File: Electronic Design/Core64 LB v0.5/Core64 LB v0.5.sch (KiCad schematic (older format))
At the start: 14 parts, among them J12 TEENSY Cur. Mon., J4 PRG, U2 Teensy3.2

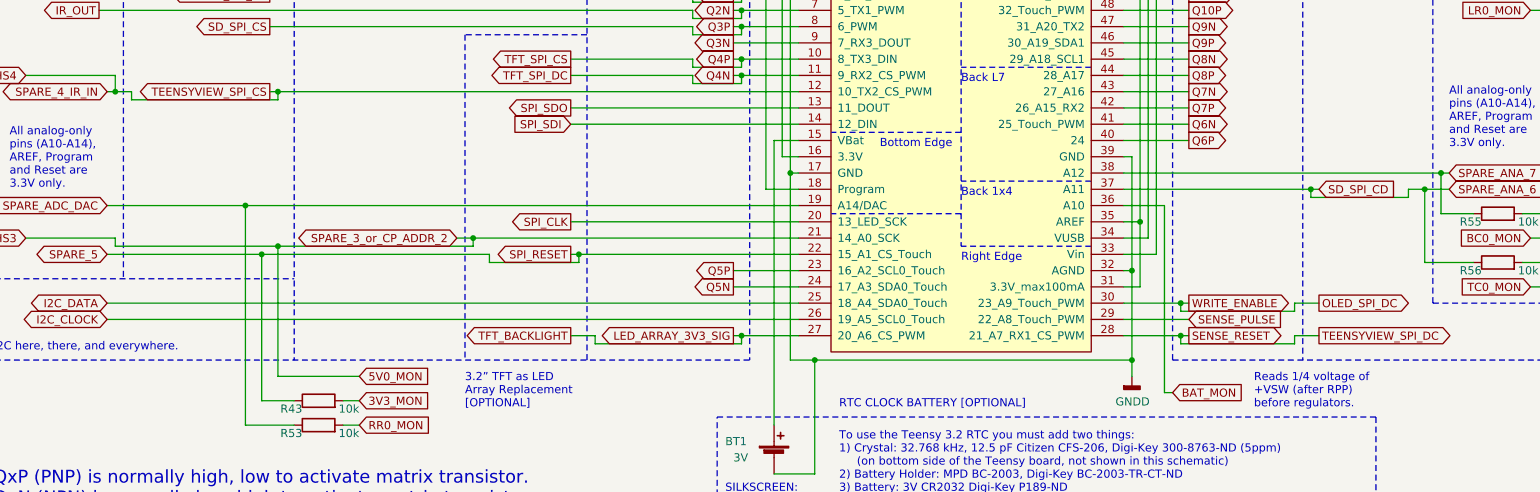
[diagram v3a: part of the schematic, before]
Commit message: Update schematic battery and LiPo charger notes, move SD_CD from ANA_6 to SPARE_3, schematic red lines
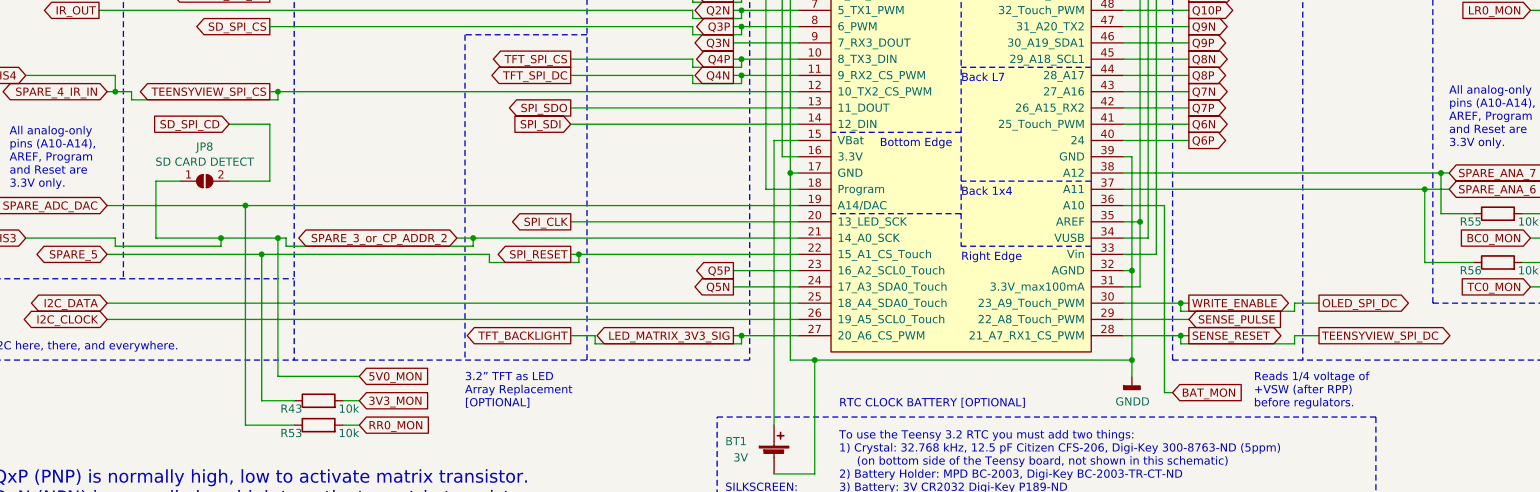
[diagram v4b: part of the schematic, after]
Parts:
- added JP8: SD CARD DETECT, Jumper:SolderJumper-2_P1.3mm_Open_RoundedPad1.0x1.5mm, symbol Jumper:SolderJumper_2_Open
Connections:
- net 5V0_MON: now also JP8.1 (A)
- net SD_SPI_CD: now also JP8.2 (B); no longer R56.1, U2.37 (A11)
- net LED_ARRAY_3V3_SIG renamed LED_MATRIX_3V3_SIG
- new net SPARE_ANA_6: R56.1, U2.37 (A11)
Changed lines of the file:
@@
 Date "2021-02-04"
 Rev "0.5"
-Comp "www.Core64.io"
-Comment1 "Work in progress"
-Comment2 "Andy Geppert"
+Comp "Concept and design by Andy Geppert @ www.MachineIdeas.com"
+Comment1 "Visit www.Core64.io for information on assembly and optional features."
+Comment2 "*** Work in progress ***"
 Comment3 ""
-Comment4 ""
+Comment4 "All non-polarized capacitors are X7R or X5R ceramic unless otherwise noted."
 $EndDescr
 Text Notes 2650 700  0    118  ~ 0
@@
 I2C_DATA
 Text GLabel 5250 5350 0    50   Output ~ 0
-LED_ARRAY_3V3_SIG
+LED_MATRIX_3V3_SIG
 $Sheet
 S 750  850  1450 250
@@
 Text GLabel 4250 4650 0    50   Output ~ 0
 SPI_CLK
-Text GLabel 8850 4450 2    50   Input ~ 0
+Text GLabel 2150 4050 0    50   Input ~ 0
 SD_SPI_CD
 $Comp
@@
 	7650 4350 9600 4350
 Wire Wire Line
-	8850 4450 8800 4450
-Wire Wire Line
 	7650 5250 8050 5250
 Wire Wire Line
@@
 Text GLabel 9650 4450 2    50   Input ~ 0
 SPARE_ANA_6
-Wire Wire Line
-	8800 4450 8800 4500
-Wire Wire Line
-	8800 4500 9400 4500
-Wire Wire Line
-	9400 4500 9400 4450
-Wire Wire Line
-	9400 4450 9500 4450
-Connection ~ 8800 4450
-Wire Wire Line
-	8800 4450 7650 4450
 Text Notes 700  6400 0    79   ~ 0
 QxP (PNP) is normally high, low to activate matrix transistor.\nQxN (NPN) is normally low, high to activate matrix transistor.
@@
 	3650 4750 3650 4800
 Wire Wire Line
-	3650 4800 2450 4800
-Wire Wire Line
 	1450 4800 1450 4750
 Wire Wire Line
@@
 Text GLabel 2950 5750 2    50   Input ~ 0
 3V3_MON
-Wire Wire Line
-	2450 4800 2450 5600
-Connection ~ 2450 4800
-Wire Wire Line
-	2450 4800 1450 4800
 Wire Wire Line
 	2350 4850 2350 5750
@@
 Wire Wire Line
 	10250 5050 10150 5050
+Wire Wire Line
+	2500 4750 2450 4750
+Wire Wire Line
+	3650 4800 2500 4800
+Wire Wire Line
+	2500 4800 2500 4750
+Wire Wire Line
+	2450 4750 2450 5600
+Connection ~ 2450 4750
+Wire Wire Line
+	2450 4750 2100 4750
+Wire Wire Line
+	2100 4750 2100 4800
+Wire Wire Line
+	2100 4800 1450 4800
+Connection ~ 2100 4750
+Wire Wire Line
+	7650 4450 9500 4450
+$Comp
+L Jumper:SolderJumper_2_Open JP8
+U 1 1 604A327B
+P 2000 4400
+F 0 "JP8" H 2000 4611 50  0000 C CNN
+F 1 "SD CARD DETECT" H 2000 4518 50  0000 C CNN
+F 2 "Jumper:SolderJumper-2_P1.3mm_Open_RoundedPad1.0x1.5mm" H 2000 4400 50  0001 C CNN
+F 3 "~" H 2000 4400 50  0001 C CNN
+	1    2000 4400
+	1    0    0    -1
+$EndComp
+Wire Wire Line
+	2150 4050 2400 4050
+Wire Wire Line
+	2400 4050 2400 4400
+Wire Wire Line
+	2400 4400 2150 4400
+Wire Wire Line
+	1850 4400 1700 4400
+Wire Wire Line
+	1700 4400 1700 4750
+Wire Wire Line
+	1700 4750 2100 4750
 $EndSCHEMATC

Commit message: Refine and release LB and CB V0.5 layout for prototyping
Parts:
- removed L3: Core_64_MachineIdeas_Link, Core_Memory_8x8_Array:Core64_QR_Link_MachineIdeas, symbol CORE_64_LIBRARY:Core_64_MachineIdeas_Link
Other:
- note removed: "All non-polarized capacitors are X7R or X5R ceramic unless otherwise noted."
- note removed: "BOM TO DO: TEENSY requires at least three headers\nthat do not get auto populated in the BOM from KiCAD."
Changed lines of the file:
@@
 Sheet 1 5
 Title "Core 64 - Main Sheet Index"
-Date "2021-02-04"
+Date "2021-02-27"
 Rev "0.5"
 Comp "Concept and design by Andy Geppert @ www.MachineIdeas.com"
 Comment1 "Visit www.Core64.io for information on assembly and optional features."
-Comment2 "*** Work in progress ***"
+Comment2 "*** As prototyped. ***"
 Comment3 ""
 Comment4 "All non-polarized capacitors are X7R or X5R ceramic unless otherwise noted."
@@
 Text Notes 650  2400 0    236  ~ 0
 TEENSY 3.2 MCU\nCONNECTIONS
-Text Notes 6350 6950 0    50   ~ 10
-BOM TO DO: TEENSY requires at least three headers\nthat do not get auto populated in the BOM from KiCAD.
 Text GLabel 4250 4650 0    50   Output ~ 0
 SPI_CLK
@@
 Text GLabel 7950 2100 2    50   Output ~ 0
 TEENSY_VUSB
-Text Notes 6300 6750 0    50   ~ 0
-All non-polarized capacitors are X7R or X5R ceramic unless otherwise noted.
 Text GLabel 5250 3050 0    50   Output ~ 0
 Q1P
@@
 Wire Wire Line
 	8700 5150 8850 5150
-$Comp
-L CORE_64_LIBRARY:Core_64_MachineIdeas_Link L3
-U 1 1 5FC1C28E
-P 5150 7200
-F 0 "L3" H 5175 7247 50  0000 L CNN
-F 1 "Core_64_MachineIdeas_Link" H 5175 7154 50  0000 L CNN
-F 2 "Core_Memory_8x8_Array:Core64_QR_Link_MachineIdeas" H 5150 7200 50  0001 C CNN
-F 3 "" H 5150 7200 50  0001 C CNN
-	1    5150 7200
-	1    0    0    -1
-$EndComp
 $Sheet
 S 3450 850  1550 250
